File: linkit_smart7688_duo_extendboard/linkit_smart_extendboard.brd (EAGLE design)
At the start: 100 x 78 mm, 28 parts, among them U1 BME280

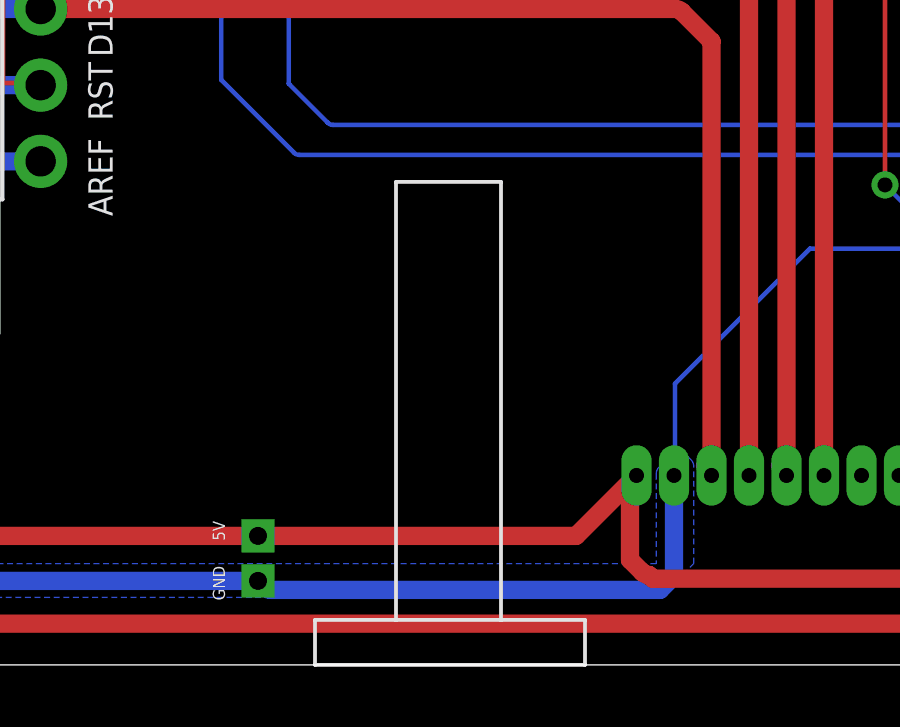
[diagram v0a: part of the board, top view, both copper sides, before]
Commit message: add gitignore, update eagle PCB
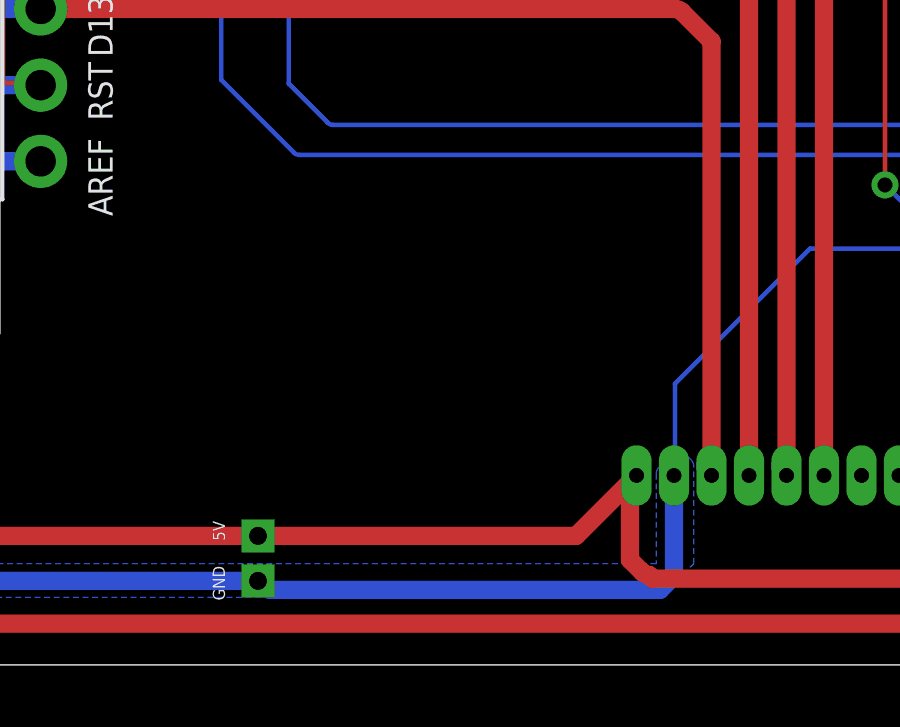
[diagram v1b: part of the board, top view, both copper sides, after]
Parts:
- removed U$6: (no value), sma:SMA
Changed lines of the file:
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@@
 </class>
 </classes>
-<designrules name="seeedstudio_dru *">
+<designrules name="jetpcb *">
 <description language="de">&lt;b&gt;EAGLE Design Rules&lt;/b&gt;
 &lt;p&gt;
@@
 <param name="mtCopper" value="0.035mm 0.035mm 0.035mm 0.035mm 0.035mm 0.035mm 0.035mm 0.035mm 0.035mm 0.035mm 0.035mm 0.035mm 0.035mm 0.035mm 0.035mm 0.035mm"/>
 <param name="mtIsolate" value="1.5mm 0.15mm 0.2mm 0.15mm 0.2mm 0.15mm 0.2mm 0.15mm 0.2mm 0.15mm 0.2mm 0.15mm 0.2mm 0.15mm 0.2mm"/>
-<param name="mdWireWire" value="6mil"/>
-<param name="mdWirePad" value="6mil"/>
-<param name="mdWireVia" value="6mil"/>
-<param name="mdPadPad" value="6mil"/>
-<param name="mdPadVia" value="6mil"/>
-<param name="mdViaVia" value="6mil"/>
-<param name="mdSmdPad" value="6mil"/>
-<param name="mdSmdVia" value="6mil"/>
-<param name="mdSmdSmd" value="6mil"/>
+<param name="mdWireWire" value="5mil"/>
+<param name="mdWirePad" value="5mil"/>
+<param name="mdWireVia" value="5mil"/>
+<param name="mdPadPad" value="5mil"/>
+<param name="mdPadVia" value="5mil"/>
+<param name="mdViaVia" value="5mil"/>
+<param name="mdSmdPad" value="5mil"/>
+<param name="mdSmdVia" value="5mil"/>
+<param name="mdSmdSmd" value="5mil"/>
 <param name="mdViaViaSameLayer" value="8mil"/>
 <param name="mnLayersViaInSmd" value="2"/>
-<param name="mdCopperDimension" value="16mil"/>
-<param name="mdDrill" value="10mil"/>
+<param name="mdCopperDimension" value="0mil"/>
+<param name="mdDrill" value="0.2499375mm"/>
 <param name="mdSmdStop" value="0mil"/>
-<param name="msWidth" value="6mil"/>
-<param name="msDrill" value="12mil"/>
+<param name="msWidth" value="5mil"/>
+<param name="msDrill" value="0.2499375mm"/>
 <param name="msMicroVia" value="9.99mm"/>
 <param name="msBlindViaRatio" value="0.5"/>
@@
 <param name="srMaxRoundness" value="0mil"/>
 <param name="slThermalIsolate" value="10mil"/>
-<param name="slThermalsForVias" value="1"/>
+<param name="slThermalsForVias" value="0"/>
 <param name="dpMaxLengthDifference" value="10mm"/>
 <param name="dpGapFactor" value="2.5"/>
@@
 <element name="U$2" library="G5" package="G5" value="" x="99.9825" y="9.0325" smashed="yes" rot="R180"/>
 <element name="U$4" library="pin_2mm" package="PIN2MM" value="PIN2MM" x="39.1" y="4.8" smashed="yes" rot="R270"/>
-<element name="U$6" library="sma" package="SMA" value="" x="41.5" y="0"/>
 </elements>
 <signals>

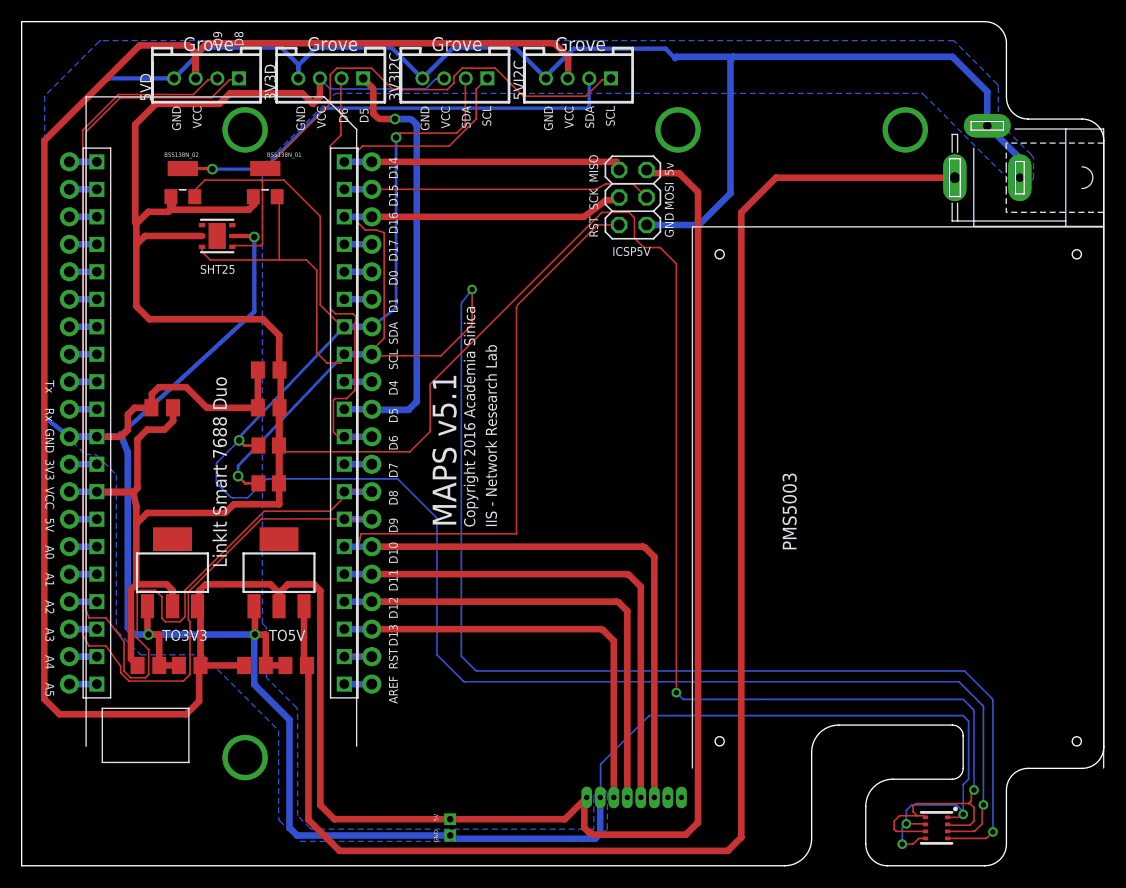
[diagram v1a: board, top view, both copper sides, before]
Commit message: add dimension in 3dm, remove 5v LDO on .brd & sch .file we don't need them any more, because the DC in is already 5v
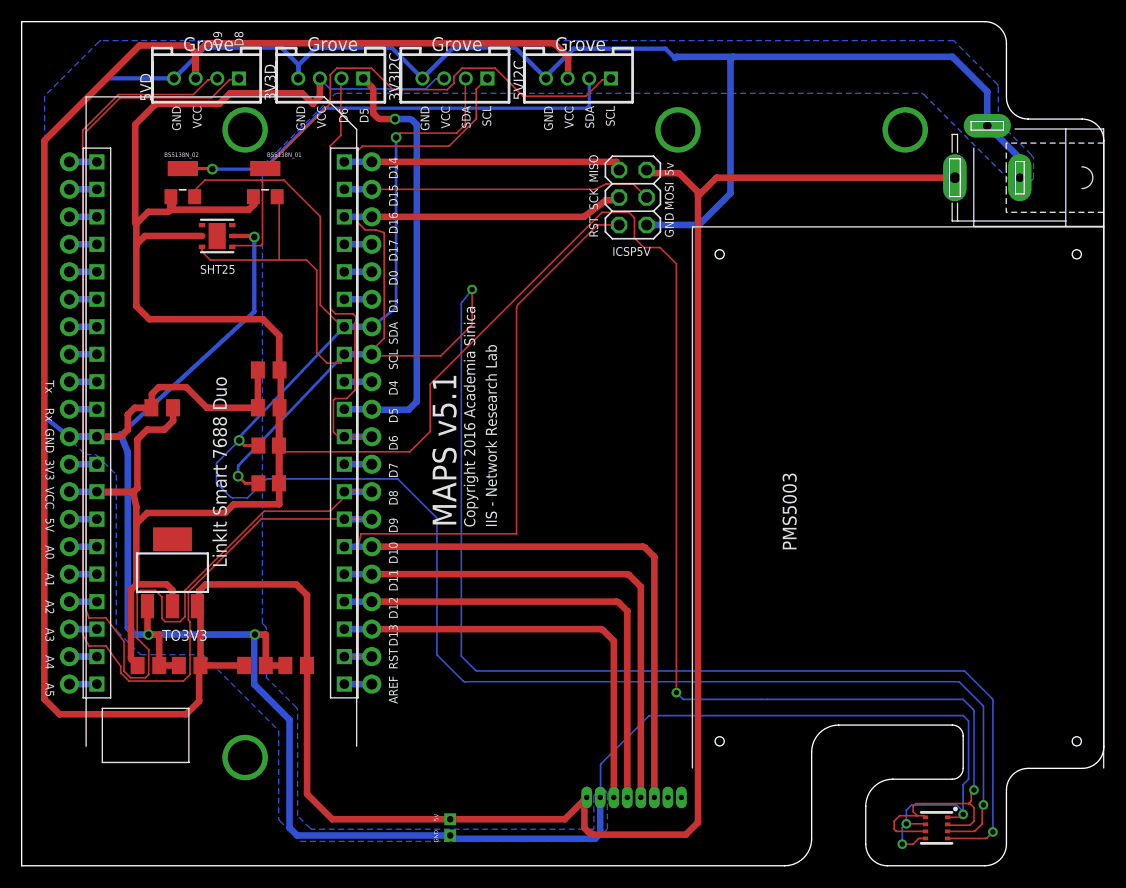
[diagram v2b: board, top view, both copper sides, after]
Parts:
- removed TO5V: LM2936MP-3.0, national-semiconductor:SOT223
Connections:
- removed net B$1: C2.1, POWER.3, TO5V.3
- removed net GND2: TO5V.4
- net +5V: now also C2.1, POWER.3; no longer TO5V.2
- net GND: no longer TO5V.1
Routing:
- net B$1: track 140.6 -> 0.00 mm
- net +5V: track 280.0 -> 300.5 mm
- net GND: track 377.7 -> 375.0 mm
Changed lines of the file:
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@@
 <attribute name="NAME" x="12.9875" y="20.7808" size="1.016" layer="25"/>
-</element>
-<element name="TO5V" library="national-semiconductor" package="SOT223" value="LM2936MP-3.0" x="23.7825" y="27.08" smashed="yes">
-<attribute name="OC_NEWARK" value="41K4522" x="23.7825" y="27.08" size="1.778" layer="27" display="off"/>
-<attribute name="MPN" value="LM2936MP-3.0/NOPB" x="23.7825" y="27.08" size="1.778" layer="27" display="off"/>
-<attribute name="MF" value="NATIONAL SEMICONDUCTOR" x="23.7825" y="27.08" size="1.778" layer="27" display="off"/>
-<attribute name="OC_FARNELL" value="1496125" x="23.7825" y="27.08" size="1.778" layer="27" display="off"/>
-<attribute name="NAME" x="22.83" y="20.7808" size="1.016" layer="25"/>
 </element>
 <element name="U$1" library="linkit7688" package="LINKIT7688" value="LINKIT7688" x="6.955" y="65.045" smashed="yes"/>
@@
 <contactref element="5VD" pad="VCC"/>
 <contactref element="5VI2C" pad="VCC"/>
-<contactref element="TO5V" pad="2"/>
 <contactref element="C1" pad="1"/>
 <contactref element="PMS3003" pad="8"/>
@@
 <wire x1="20.56" y1="18.5075" x2="16.5275" y2="18.5075" width="0.6096" layer="1"/>
 <contactref element="U$4" pad="5V"/>
-<wire x1="23.7825" y1="23.9812" x2="23.7825" y2="25.1825" width="0.6096" layer="1"/>
-<wire x1="23.7825" y1="25.1825" x2="24.6" y2="26" width="0.6096" layer="1"/>
-<wire x1="24.6" y1="26" x2="27" y2="26" width="0.6096" layer="1"/>
-<wire x1="27" y1="26" x2="27.6" y2="25.4" width="0.6096" layer="1"/>
-<wire x1="27.6" y1="25.4" x2="27.6" y2="5.6" width="0.6096" layer="1"/>
-<wire x1="27.6" y1="5.6" x2="28.9" y2="4.3" width="0.6096" layer="1"/>
-<wire x1="28.9" y1="4.3" x2="39.6" y2="4.3" width="0.6096" layer="1"/>
-<wire x1="23.7825" y1="23.9812" x2="23.7825" y2="25.2175" width="0.6096" layer="1"/>
-<wire x1="23.7825" y1="25.2175" x2="23" y2="26" width="0.6096" layer="1"/>
-<wire x1="23" y1="26" x2="17" y2="26" width="0.6096" layer="1"/>
+<wire x1="28.7" y1="4.3" x2="39.6" y2="4.3" width="0.6096" layer="1"/>
 <wire x1="17" y1="26" x2="16.4" y2="25.4" width="0.6096" layer="1"/>
 <wire x1="16.4" y1="25.4" x2="16.4" y2="24.1298" width="0.6096" layer="1"/>
@@
 <wire x1="58.045" y1="64" x2="60.75" y2="64" width="0.6096" layer="1"/>
 <wire x1="60.75" y1="64" x2="62.5" y2="62.25" width="0.6096" layer="1"/>
-<wire x1="62.5" y1="62.25" x2="62.5" y2="4" width="0.6096" layer="1"/>
+<wire x1="62.5" y1="62.25" x2="62.5" y2="61.875" width="0.6096" layer="1"/>
+<wire x1="62.5" y1="61.875" x2="62.5" y2="4" width="0.6096" layer="1"/>
 <wire x1="62.5" y1="4" x2="61.375" y2="2.875" width="0.6096" layer="1"/>
 <wire x1="61.375" y1="2.875" x2="52.7565125" y2="2.875" width="0.6096" layer="1"/>
 <wire x1="52.7565125" y1="2.875" x2="52.6315125" y2="3" width="0.6096" layer="1"/>
+<contactref element="POWER" pad="3"/>
+<contactref element="C2" pad="1"/>
+<wire x1="86.231" y1="63.58" x2="64.205" y2="63.58" width="0.6096" layer="1"/>
+<wire x1="64.205" y1="63.58" x2="62.5" y2="61.875" width="0.6096" layer="1"/>
+<wire x1="28.7" y1="4.3" x2="26.375" y2="6.625" width="0.6096" layer="1"/>
+<wire x1="26.375" y1="6.625" x2="26.375" y2="18.5025" width="0.6096" layer="1"/>
+<wire x1="26.375" y1="18.5025" x2="26.37" y2="18.5075" width="0.6096" layer="1"/>
+<wire x1="26.37" y1="18.5075" x2="26.37" y2="25.005" width="0.6096" layer="1"/>
+<wire x1="26.37" y1="25.005" x2="25.375" y2="26" width="0.6096" layer="1"/>
+<wire x1="25.375" y1="26" x2="17" y2="26" width="0.6096" layer="1"/>
 </signal>
 <signal name="+3V3">
@@
 <contactref element="5VI2C" pad="GND"/>
 <contactref element="TO3V3" pad="1"/>
-<contactref element="TO5V" pad="1"/>
 <contactref element="POWER" pad="1"/>
 <contactref element="POWER" pad="2"/>
@@
 <contactref element="C6" pad="2"/>
 <contactref element="C7" pad="2"/>
-<wire x1="21.4711" y1="23.9812" x2="21.56" y2="23.9812" width="0.6096" layer="1"/>
-<wire x1="21.56" y1="23.9812" x2="21.56" y2="21.365" width="0.6096" layer="1"/>
 <via x="21.56" y="21.365" extent="1-16" drill="0.6" shape="square"/>
 <wire x1="24.37" y1="18.5075" x2="22.56" y2="18.5075" width="0.6096" layer="1"/>
@@
 <wire x1="32.42060625" y1="47.19939375" x2="32.355" y2="47.265" width="0.1524" layer="1"/>
 </signal>
-<signal name="B$1">
-<contactref element="TO5V" pad="3"/>
-<contactref element="C2" pad="1"/>
-<contactref element="POWER" pad="3"/>
-<wire x1="26.37" y1="18.5075" x2="26.0939" y2="18.5075" width="0.6096" layer="1"/>
-<wire x1="26.0939" y1="18.5075" x2="26.0939" y2="23.9812" width="0.6096" layer="1"/>
-<wire x1="86.231" y1="63.58" x2="69.705" y2="63.58" width="0.6096" layer="1"/>
-<wire x1="69.705" y1="63.58" x2="66.5" y2="60.375" width="0.6096" layer="1"/>
-<wire x1="66.5" y1="60.375" x2="66.5" y2="2.625" width="0.6096" layer="1"/>
-<wire x1="66.5" y1="2.625" x2="65.25" y2="1.375" width="0.6096" layer="1"/>
-<wire x1="65.25" y1="1.375" x2="29.375" y2="1.375" width="0.6096" layer="1"/>
-<wire x1="29.375" y1="1.375" x2="26.5" y2="4.25" width="0.6096" layer="1"/>
-<wire x1="26.5" y1="4.25" x2="26.5" y2="18.3775" width="0.6096" layer="1"/>
-<wire x1="26.5" y1="18.3775" x2="26.37" y2="18.5075" width="0.6096" layer="1"/>
-</signal>
 <signal name="N$20">
 <contactref element="U$1" pad="P$1.P0"/>
@@
 <contactref element="TO3V3" pad="4"/>
 </signal>
-<signal name="GND2">
-<contactref element="TO5V" pad="4"/>
-</signal>
 <signal name="N$2">
